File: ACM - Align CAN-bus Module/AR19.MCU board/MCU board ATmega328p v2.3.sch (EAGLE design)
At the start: 39 parts, among them IC1 ATMEGA328P-MMH, IC2 MIC5239-5.0YS_TR, IC3 MCP25625-E_ML, J1 AVR_SPI_PROG_3X2NS

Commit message: Ryddet og la til den nye krystallen
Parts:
- removed QF1, QF2: 16M20AUM1, crystal:16M20AUM1
- added U$1, U$2: FA-20H, FA-20H 16.0000MF20X-B:FA-20H
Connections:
- net CAN_OSC1: now also U$1.1; no longer QF2.1
- net CAN_OSC2: now also U$1.3; no longer QF2.3
- net GND: no longer QF1.2, QF2.2
- net MCU_OSC1: now also U$2.1; no longer QF1.1
- net MCU_OSC2: now also U$2.3; no longer QF1.3
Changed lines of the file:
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@@
 <part name="C2" library="12066D106KAT2A" deviceset="12066D106KAT2A" device="" value="22pF"/>
 <part name="C3" library="12066D106KAT2A" deviceset="12066D106KAT2A" device="" value="22pF"/>
-<part name="GND1" library="supply1" library_urn="urn:adsk.eagle:library:371" deviceset="GND" device=""/>
 <part name="GND2" library="supply1" library_urn="urn:adsk.eagle:library:371" deviceset="GND" device=""/>
 <part name="P_I/O6" library="wirepad" library_urn="urn:adsk.eagle:library:412" deviceset="2,15/1,0" device="" package3d_urn="urn:adsk.eagle:package:30831/1"/>
@@
 <part name="GND5" library="supply1" library_urn="urn:adsk.eagle:library:371" deviceset="GND" device=""/>
 <part name="GND6" library="supply1" library_urn="urn:adsk.eagle:library:371" deviceset="GND" device=""/>
-<part name="QF1" library="crystal" library_urn="urn:adsk.eagle:library:204" deviceset="16M20AUM1" device="" package3d_urn="urn:adsk.eagle:package:12117/1"/>
 <part name="CAN_H" library="wirepad" library_urn="urn:adsk.eagle:library:412" deviceset="2,15/1,0" device="" package3d_urn="urn:adsk.eagle:package:30831/1"/>
 <part name="CAN_L" library="wirepad" library_urn="urn:adsk.eagle:library:412" deviceset="2,15/1,0" device="" package3d_urn="urn:adsk.eagle:package:30831/1"/>
@@
 <part name="C9" library="12066D106KAT2A" deviceset="12066D106KAT2A" device="" value="22pF"/>
 <part name="C10" library="12066D106KAT2A" deviceset="12066D106KAT2A" device="" value="22pF"/>
-<part name="GND19" library="supply1" library_urn="urn:adsk.eagle:library:371" deviceset="GND" device=""/>
-<part name="QF2" library="crystal" library_urn="urn:adsk.eagle:library:204" deviceset="16M20AUM1" device="" package3d_urn="urn:adsk.eagle:package:12117/1"/>
 <part name="GND20" library="supply1" library_urn="urn:adsk.eagle:library:371" deviceset="GND" device=""/>
 <part name="GND21" library="supply1" library_urn="urn:adsk.eagle:library:371" deviceset="GND" device=""/>
+<part name="U$1" library="FA-20H 16.0000MF20X-B" deviceset="FA-20H" device=""/>
+<part name="U$2" library="FA-20H 16.0000MF20X-B" deviceset="FA-20H" device=""/>
 </parts>
 <sheets>
@@
 <attribute name="VALUE" x="354.33" y="95.25" size="1.778" layer="96" rot="R180" align="center-left"/>
 </instance>
-<instance part="GND1" gate="1" x="332.74" y="81.28" smashed="yes">
-<attribute name="VALUE" x="330.2" y="78.74" size="1.778" layer="96"/>
-</instance>
 <instance part="GND2" gate="1" x="-22.86" y="142.24" smashed="yes">
 <attribute name="VALUE" x="-25.4" y="139.7" size="1.778" layer="96"/>
@@
 <attribute name="VALUE" x="-27.94" y="139.7" size="1.778" layer="96" rot="MR0"/>
 </instance>
-<instance part="QF1" gate="G$1" x="332.74" y="101.6" smashed="yes">
-<attribute name="NAME" x="332.74" y="110.236" size="1.778" layer="95"/>
-<attribute name="VALUE" x="332.74" y="106.68" size="1.778" layer="96"/>
-</instance>
 <instance part="CAN_H" gate="1" x="238.76" y="5.08" smashed="yes" rot="R180">
 <attribute name="NAME" x="239.903" y="8.3058" size="1.778" layer="95" rot="R180"/>
@@
 <attribute name="VALUE" x="349.25" y="57.15" size="1.778" layer="96" align="center-left"/>
 </instance>
-<instance part="GND19" gate="1" x="332.74" y="48.26" smashed="yes">
-<attribute name="VALUE" x="330.2" y="45.72" size="1.778" layer="96"/>
-</instance>
-<instance part="QF2" gate="G$1" x="332.74" y="68.58" smashed="yes">
-<attribute name="NAME" x="335.28" y="69.596" size="1.778" layer="95"/>
-<attribute name="VALUE" x="335.28" y="66.04" size="1.778" layer="96"/>
-</instance>
 <instance part="GND20" gate="1" x="320.04" y="48.26" smashed="yes">
 <attribute name="VALUE" x="317.5" y="45.72" size="1.778" layer="96"/>
@@
 <attribute name="VALUE" x="342.9" y="45.72" size="1.778" layer="96"/>
 </instance>
+<instance part="U$1" gate="G$1" x="363.22" y="55.88" smashed="yes"/>
+<instance part="U$2" gate="G$1" x="363.22" y="88.9" smashed="yes"/>
 </instances>
 <busses>
@@
 </segment>
 <segment>
-<pinref part="GND1" gate="1" pin="GND"/>
-<pinref part="QF1" gate="G$1" pin="2"/>
-<wire x1="332.74" y1="83.82" x2="332.74" y2="96.52" width="0.1524" layer="91"/>
-</segment>
-<segment>
 <pinref part="C2" gate="G$1" pin="1"/>
 <pinref part="GND17" gate="1" pin="GND"/>
@@
 <pinref part="GND18" gate="1" pin="GND"/>
 <wire x1="345.44" y1="86.36" x2="345.44" y2="83.82" width="0.1524" layer="91"/>
-</segment>
-<segment>
-<pinref part="GND19" gate="1" pin="GND"/>
-<pinref part="QF2" gate="G$1" pin="2"/>
-<wire x1="332.74" y1="50.8" x2="332.74" y2="63.5" width="0.1524" layer="91"/>
 </segment>
 <segment>
@@
 <pinref part="C2" gate="G$1" pin="2"/>
 <label x="314.96" y="101.6" size="1.778" layer="95" rot="R180"/>
-<pinref part="QF1" gate="G$1" pin="1"/>
 <wire x1="320.04" y1="99.06" x2="320.04" y2="101.6" width="0.1524" layer="91"/>
-<wire x1="320.04" y1="101.6" x2="330.2" y2="101.6" width="0.1524" layer="91"/>
 <wire x1="320.04" y1="101.6" x2="314.96" y2="101.6" width="0.1524" layer="91"/>
+<pinref part="U$2" gate="G$1" pin="1"/>
+<wire x1="320.04" y1="101.6" x2="322.58" y2="101.6" width="0.1524" layer="91"/>
 <junction x="320.04" y="101.6"/>
 </segment>
@@
 <pinref part="C3" gate="G$1" pin="2"/>
 <label x="350.52" y="101.6" size="1.778" layer="95" rot="MR180"/>
-<pinref part="QF1" gate="G$1" pin="3"/>
 <wire x1="345.44" y1="99.06" x2="345.44" y2="101.6" width="0.1524" layer="91"/>
-<wire x1="345.44" y1="101.6" x2="335.28" y2="101.6" width="0.1524" layer="91"/>
 <wire x1="345.44" y1="101.6" x2="350.52" y2="101.6" width="0.1524" layer="91"/>
+<pinref part="U$2" gate="G$1" pin="3"/>
+<wire x1="339.09" y1="101.6" x2="345.44" y2="101.6" width="0.1524" layer="91"/>
 <junction x="345.44" y="101.6"/>
 </segment>
@@
 <pinref part="C9" gate="G$1" pin="2"/>
 <label x="314.96" y="68.58" size="1.778" layer="95" rot="R180"/>
-<pinref part="QF2" gate="G$1" pin="1"/>
 <wire x1="320.04" y1="66.04" x2="320.04" y2="68.58" width="0.1524" layer="91"/>
-<wire x1="320.04" y1="68.58" x2="330.2" y2="68.58" width="0.1524" layer="91"/>
 <wire x1="320.04" y1="68.58" x2="314.96" y2="68.58" width="0.1524" layer="91"/>
+<pinref part="U$1" gate="G$1" pin="1"/>
+<wire x1="322.58" y1="68.58" x2="320.04" y2="68.58" width="0.1524" layer="91"/>
 <junction x="320.04" y="68.58"/>
 </segment>
@@
 <pinref part="C10" gate="G$1" pin="2"/>
 <label x="350.52" y="68.58" size="1.778" layer="95" rot="MR180"/>
-<pinref part="QF2" gate="G$1" pin="3"/>
 <wire x1="345.44" y1="66.04" x2="345.44" y2="68.58" width="0.1524" layer="91"/>
-<wire x1="345.44" y1="68.58" x2="335.28" y2="68.58" width="0.1524" layer="91"/>
 <wire x1="345.44" y1="68.58" x2="350.52" y2="68.58" width="0.1524" layer="91"/>
+<pinref part="U$1" gate="G$1" pin="3"/>
+<wire x1="339.09" y1="68.58" x2="345.44" y2="68.58" width="0.1524" layer="91"/>
 <junction x="345.44" y="68.58"/>
 </segment>

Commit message: Pakket og klart
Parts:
- removed U$1, U$2: FA-20H, FA-20H 16.0000MF20X-B:FA-20H
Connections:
- net CAN_OSC1: no longer U$1.1
- net CAN_OSC2: no longer U$1.3
- net MCU_OSC1: no longer U$2.1
- net MCU_OSC2: no longer U$2.3
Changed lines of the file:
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@@
 <part name="GND20" library="supply1" library_urn="urn:adsk.eagle:library:371" deviceset="GND" device=""/>
 <part name="GND21" library="supply1" library_urn="urn:adsk.eagle:library:371" deviceset="GND" device=""/>
-<part name="U$1" library="FA-20H 16.0000MF20X-B" deviceset="FA-20H" device=""/>
-<part name="U$2" library="FA-20H 16.0000MF20X-B" deviceset="FA-20H" device=""/>
 </parts>
 <sheets>
@@
 <attribute name="VALUE" x="342.9" y="45.72" size="1.778" layer="96"/>
 </instance>
-<instance part="U$1" gate="G$1" x="363.22" y="55.88" smashed="yes"/>
-<instance part="U$2" gate="G$1" x="363.22" y="88.9" smashed="yes"/>
 </instances>
 <busses>
@@
 <label x="314.96" y="101.6" size="1.778" layer="95" rot="R180"/>
 <wire x1="320.04" y1="99.06" x2="320.04" y2="101.6" width="0.1524" layer="91"/>
+<wire x1="320.04" y1="101.6" x2="330.2" y2="101.6" width="0.1524" layer="91"/>
 <wire x1="320.04" y1="101.6" x2="314.96" y2="101.6" width="0.1524" layer="91"/>
-<pinref part="U$2" gate="G$1" pin="1"/>
-<wire x1="320.04" y1="101.6" x2="322.58" y2="101.6" width="0.1524" layer="91"/>
 <junction x="320.04" y="101.6"/>
 </segment>
@@
 <label x="350.52" y="101.6" size="1.778" layer="95" rot="MR180"/>
 <wire x1="345.44" y1="99.06" x2="345.44" y2="101.6" width="0.1524" layer="91"/>
+<wire x1="345.44" y1="101.6" x2="335.28" y2="101.6" width="0.1524" layer="91"/>
 <wire x1="345.44" y1="101.6" x2="350.52" y2="101.6" width="0.1524" layer="91"/>
-<pinref part="U$2" gate="G$1" pin="3"/>
-<wire x1="339.09" y1="101.6" x2="345.44" y2="101.6" width="0.1524" layer="91"/>
 <junction x="345.44" y="101.6"/>
 </segment>
@@
 <label x="314.96" y="68.58" size="1.778" layer="95" rot="R180"/>
 <wire x1="320.04" y1="66.04" x2="320.04" y2="68.58" width="0.1524" layer="91"/>
+<wire x1="320.04" y1="68.58" x2="330.2" y2="68.58" width="0.1524" layer="91"/>
 <wire x1="320.04" y1="68.58" x2="314.96" y2="68.58" width="0.1524" layer="91"/>
-<pinref part="U$1" gate="G$1" pin="1"/>
-<wire x1="322.58" y1="68.58" x2="320.04" y2="68.58" width="0.1524" layer="91"/>
 <junction x="320.04" y="68.58"/>
 </segment>
@@
 <label x="350.52" y="68.58" size="1.778" layer="95" rot="MR180"/>
 <wire x1="345.44" y1="66.04" x2="345.44" y2="68.58" width="0.1524" layer="91"/>
+<wire x1="345.44" y1="68.58" x2="335.28" y2="68.58" width="0.1524" layer="91"/>
 <wire x1="345.44" y1="68.58" x2="350.52" y2="68.58" width="0.1524" layer="91"/>
-<pinref part="U$1" gate="G$1" pin="3"/>
-<wire x1="339.09" y1="68.58" x2="345.44" y2="68.58" width="0.1524" layer="91"/>
 <junction x="345.44" y="68.58"/>
 </segment>

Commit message: Created BOM 031018
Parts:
- added U$1, U$2: FA-20H, FA-20H 16.0000MF20X-B:FA-20H
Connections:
- net CAN_OSC1: now also U$1.1
- net CAN_OSC2: now also U$1.3
- net MCU_OSC1: now also U$2.1
- net MCU_OSC2: now also U$2.3
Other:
- moved on the sheet: C10, C2, C3, C9
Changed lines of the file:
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@@
 <part name="GND20" library="supply1" library_urn="urn:adsk.eagle:library:371" deviceset="GND" device=""/>
 <part name="GND21" library="supply1" library_urn="urn:adsk.eagle:library:371" deviceset="GND" device=""/>
+<part name="U$1" library="FA-20H 16.0000MF20X-B" deviceset="FA-20H" device=""/>
+<part name="U$2" library="FA-20H 16.0000MF20X-B" deviceset="FA-20H" device=""/>
 </parts>
 <sheets>
@@
 <attribute name="VALUE" x="85.217" y="146.558" size="1.778" layer="96"/>
 </instance>
-<instance part="C2" gate="G$1" x="320.04" y="86.36" smashed="yes" rot="R90">
-<attribute name="NAME" x="316.23" y="92.71" size="1.778" layer="95" rot="R180" align="center-left"/>
-<attribute name="VALUE" x="316.23" y="95.25" size="1.778" layer="96" rot="R180" align="center-left"/>
-</instance>
-<instance part="C3" gate="G$1" x="345.44" y="86.36" smashed="yes" rot="R90">
-<attribute name="NAME" x="351.79" y="92.71" size="1.778" layer="95" rot="R180" align="center-left"/>
-<attribute name="VALUE" x="354.33" y="95.25" size="1.778" layer="96" rot="R180" align="center-left"/>
+<instance part="C2" gate="G$1" x="322.58" y="86.36" smashed="yes" rot="R90">
+<attribute name="NAME" x="318.77" y="92.71" size="1.778" layer="95" rot="R180" align="center-left"/>
+<attribute name="VALUE" x="318.77" y="95.25" size="1.778" layer="96" rot="R180" align="center-left"/>
+</instance>
+<instance part="C3" gate="G$1" x="350.52" y="86.36" smashed="yes" rot="R90">
+<attribute name="NAME" x="356.87" y="92.71" size="1.778" layer="95" rot="R180" align="center-left"/>
+<attribute name="VALUE" x="359.41" y="95.25" size="1.778" layer="96" rot="R180" align="center-left"/>
 </instance>
 <instance part="GND2" gate="1" x="-22.86" y="142.24" smashed="yes">
@@
 <attribute name="VALUE" x="226.06" y="27.94" size="1.778" layer="96"/>
 </instance>
-<instance part="GND17" gate="1" x="320.04" y="81.28" smashed="yes">
-<attribute name="VALUE" x="317.5" y="78.74" size="1.778" layer="96"/>
-</instance>
-<instance part="GND18" gate="1" x="345.44" y="81.28" smashed="yes">
-<attribute name="VALUE" x="342.9" y="78.74" size="1.778" layer="96"/>
-</instance>
-<instance part="C9" gate="G$1" x="320.04" y="53.34" smashed="yes" rot="R90">
-<attribute name="NAME" x="316.23" y="59.69" size="1.778" layer="95" rot="R180" align="center-left"/>
-<attribute name="VALUE" x="316.23" y="57.15" size="1.778" layer="96" rot="R180" align="center-left"/>
-</instance>
-<instance part="C10" gate="G$1" x="345.44" y="53.34" smashed="yes" rot="R90">
-<attribute name="NAME" x="349.25" y="59.69" size="1.778" layer="95" align="center-left"/>
-<attribute name="VALUE" x="349.25" y="57.15" size="1.778" layer="96" align="center-left"/>
-</instance>
-<instance part="GND20" gate="1" x="320.04" y="48.26" smashed="yes">
-<attribute name="VALUE" x="317.5" y="45.72" size="1.778" layer="96"/>
-</instance>
-<instance part="GND21" gate="1" x="345.44" y="48.26" smashed="yes">
-<attribute name="VALUE" x="342.9" y="45.72" size="1.778" layer="96"/>
-</instance>
+<instance part="GND17" gate="1" x="322.58" y="81.28" smashed="yes">
+<attribute name="VALUE" x="320.04" y="78.74" size="1.778" layer="96"/>
+</instance>
+<instance part="GND18" gate="1" x="350.52" y="81.28" smashed="yes">
+<attribute name="VALUE" x="347.98" y="78.74" size="1.778" layer="96"/>
+</instance>
+<instance part="C9" gate="G$1" x="322.58" y="45.72" smashed="yes" rot="R90">
+<attribute name="NAME" x="318.77" y="52.07" size="1.778" layer="95" rot="R180" align="center-left"/>
+<attribute name="VALUE" x="318.77" y="49.53" size="1.778" layer="96" rot="R180" align="center-left"/>
+</instance>
+<instance part="C10" gate="G$1" x="350.52" y="45.72" smashed="yes" rot="R90">
+<attribute name="NAME" x="354.33" y="52.07" size="1.778" layer="95" align="center-left"/>
+<attribute name="VALUE" x="354.33" y="49.53" size="1.778" layer="96" align="center-left"/>
+</instance>
+<instance part="GND20" gate="1" x="322.58" y="40.64" smashed="yes">
+<attribute name="VALUE" x="320.04" y="38.1" size="1.778" layer="96"/>
+</instance>
+<instance part="GND21" gate="1" x="350.52" y="40.64" smashed="yes">
+<attribute name="VALUE" x="347.98" y="38.1" size="1.778" layer="96"/>
+</instance>
+<instance part="U$1" gate="G$1" x="337.82" y="58.42" smashed="yes"/>
+<instance part="U$2" gate="G$1" x="335.28" y="99.06" smashed="yes"/>
 </instances>
 <busses>
@@
 <pinref part="C2" gate="G$1" pin="1"/>
 <pinref part="GND17" gate="1" pin="GND"/>
-<wire x1="320.04" y1="86.36" x2="320.04" y2="83.82" width="0.1524" layer="91"/>
+<wire x1="322.58" y1="86.36" x2="322.58" y2="83.82" width="0.1524" layer="91"/>
 </segment>
 <segment>
 <pinref part="C3" gate="G$1" pin="1"/>
 <pinref part="GND18" gate="1" pin="GND"/>
-<wire x1="345.44" y1="86.36" x2="345.44" y2="83.82" width="0.1524" layer="91"/>
+<wire x1="350.52" y1="86.36" x2="350.52" y2="83.82" width="0.1524" layer="91"/>
 </segment>
 <segment>
 <pinref part="C9" gate="G$1" pin="1"/>
 <pinref part="GND20" gate="1" pin="GND"/>
-<wire x1="320.04" y1="53.34" x2="320.04" y2="50.8" width="0.1524" layer="91"/>
+<wire x1="322.58" y1="45.72" x2="322.58" y2="43.18" width="0.1524" layer="91"/>
 </segment>
 <segment>
 <pinref part="C10" gate="G$1" pin="1"/>
 <pinref part="GND21" gate="1" pin="GND"/>
-<wire x1="345.44" y1="53.34" x2="345.44" y2="50.8" width="0.1524" layer="91"/>
+<wire x1="350.52" y1="45.72" x2="350.52" y2="43.18" width="0.1524" layer="91"/>
 </segment>
 </net>
@@
 <segment>
 <pinref part="C2" gate="G$1" pin="2"/>
-<label x="314.96" y="101.6" size="1.778" layer="95" rot="R180"/>
-<wire x1="320.04" y1="99.06" x2="320.04" y2="101.6" width="0.1524" layer="91"/>
-<wire x1="320.04" y1="101.6" x2="330.2" y2="101.6" width="0.1524" layer="91"/>
-<wire x1="320.04" y1="101.6" x2="314.96" y2="101.6" width="0.1524" layer="91"/>
-<junction x="320.04" y="101.6"/>
+<label x="317.5" y="101.6" size="1.778" layer="95" rot="R180"/>
+<wire x1="322.58" y1="99.06" x2="322.58" y2="101.6" width="0.1524" layer="91"/>
+<wire x1="322.58" y1="101.6" x2="317.5" y2="101.6" width="0.1524" layer="91"/>
+<pinref part="U$2" gate="G$1" pin="1"/>
+<wire x1="327.04" y1="101.06" x2="327.04" y2="101.6" width="0.1524" layer="91"/>
+<wire x1="327.04" y1="101.6" x2="322.58" y2="101.6" width="0.1524" layer="91"/>
+<junction x="322.58" y="101.6"/>
 </segment>
 </net>
@@
 <segment>
 <pinref part="C3" gate="G$1" pin="2"/>
-<label x="350.52" y="101.6" size="1.778" layer="95" rot="MR180"/>
-<wire x1="345.44" y1="99.06" x2="345.44" y2="101.6" width="0.1524" layer="91"/>
-<wire x1="345.44" y1="101.6" x2="335.28" y2="101.6" width="0.1524" layer="91"/>
-<wire x1="345.44" y1="101.6" x2="350.52" y2="101.6" width="0.1524" layer="91"/>
-<junction x="345.44" y="101.6"/>
+<label x="355.6" y="101.6" size="1.778" layer="95" rot="MR180"/>
+<wire x1="350.52" y1="99.06" x2="350.52" y2="101.6" width="0.1524" layer="91"/>
+<wire x1="350.52" y1="101.6" x2="355.6" y2="101.6" width="0.1524" layer="91"/>
+<pinref part="U$2" gate="G$1" pin="3"/>
+<wire x1="343.55" y1="101.06" x2="343.55" y2="101.6" width="0.1524" layer="91"/>
+<wire x1="343.55" y1="101.6" x2="350.52" y2="101.6" width="0.1524" layer="91"/>
+<junction x="350.52" y="101.6"/>
 </segment>
 </net>
@@
 <segment>
 <pinref part="C9" gate="G$1" pin="2"/>
-<label x="314.96" y="68.58" size="1.778" layer="95" rot="R180"/>
-<wire x1="320.04" y1="66.04" x2="320.04" y2="68.58" width="0.1524" layer="91"/>
-<wire x1="320.04" y1="68.58" x2="330.2" y2="68.58" width="0.1524" layer="91"/>
-<wire x1="320.04" y1="68.58" x2="314.96" y2="68.58" width="0.1524" layer="91"/>
-<junction x="320.04" y="68.58"/>
+<label x="317.5" y="60.96" size="1.778" layer="95" rot="R180"/>
+<wire x1="322.58" y1="58.42" x2="322.58" y2="60.96" width="0.1524" layer="91"/>
+<wire x1="322.58" y1="60.96" x2="317.5" y2="60.96" width="0.1524" layer="91"/>
+<pinref part="U$1" gate="G$1" pin="1"/>
+<wire x1="329.58" y1="60.42" x2="329.58" y2="60.96" width="0.1524" layer="91"/>
+<wire x1="329.58" y1="60.96" x2="322.58" y2="60.96" width="0.1524" layer="91"/>
+<junction x="322.58" y="60.96"/>
 </segment>
 </net>
@@
 <segment>
 <pinref part="C10" gate="G$1" pin="2"/>
-<label x="350.52" y="68.58" size="1.778" layer="95" rot="MR180"/>
-<wire x1="345.44" y1="66.04" x2="345.44" y2="68.58" width="0.1524" layer="91"/>
-<wire x1="345.44" y1="68.58" x2="335.28" y2="68.58" width="0.1524" layer="91"/>
-<wire x1="345.44" y1="68.58" x2="350.52" y2="68.58" width="0.1524" layer="91"/>
-<junction x="345.44" y="68.58"/>
-</segment>
-</net>
+<label x="355.6" y="60.96" size="1.778" layer="95" rot="MR180"/>
+<wire x1="350.52" y1="58.42" x2="350.52" y2="60.96" width="0.1524" layer="91"/>
+<wire x1="350.52" y1="60.96" x2="355.6" y2="60.96" width="0.1524" layer="91"/>
+<pinref part="U$1" gate="G$1" pin="3"/>
+<wire x1="346.09" y1="60.42" x2="346.09" y2="60.96" width="0.1524" layer="91"/>
+<wire x1="346.09" y1="60.96" x2="350.52" y2="60.96" width="0.1524" layer="91"/>
+<junction x="350.52" y="60.96"/>
+</segment>
+</net>

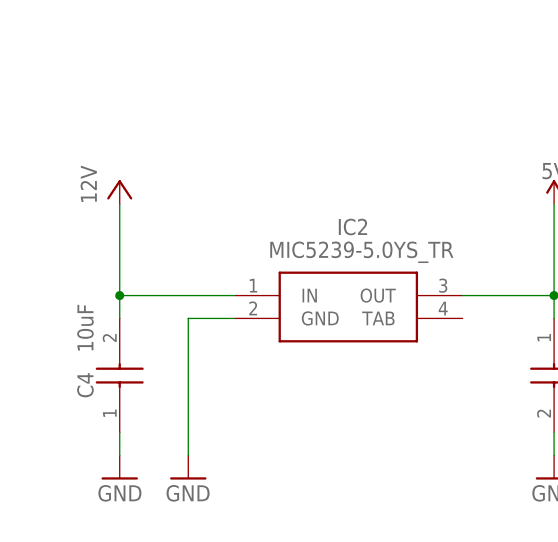
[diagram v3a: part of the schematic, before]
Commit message: Added: Fuse Block (Littelfuse SMD fuse block)
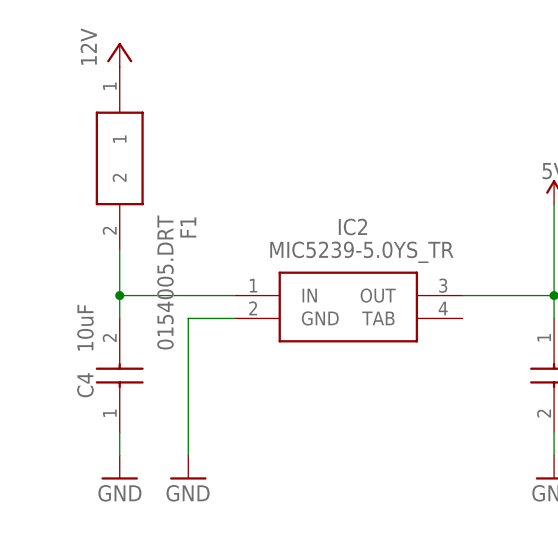
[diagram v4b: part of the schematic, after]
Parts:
- added F1: 0154005.DRT, 0154005(Fuseholder)DRT:0154005.DRT
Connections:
- new net N$2: C4.A, F1.2, IC2.IN
- net VCC: now also F1.1; no longer C4.A, IC2.IN
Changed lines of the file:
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@@
 <part name="U$1" library="FA-20H 16.0000MF20X-B" deviceset="FA-20H" device=""/>
 <part name="U$2" library="FA-20H 16.0000MF20X-B" deviceset="FA-20H" device=""/>
+<part name="F1" library="0154005(Fuseholder)DRT" deviceset="0154005.DRT" device=""/>
 </parts>
 <sheets>
@@
 <attribute name="VALUE" x="220.98" y="66.04" size="1.778" layer="96"/>
 </instance>
-<instance part="P+2" gate="VCC" x="-30.48" y="175.26" smashed="yes">
-<attribute name="VALUE" x="-33.02" y="172.72" size="1.778" layer="96" rot="R90"/>
+<instance part="P+2" gate="VCC" x="-30.48" y="190.5" smashed="yes">
+<attribute name="VALUE" x="-33.02" y="187.96" size="1.778" layer="96" rot="R90"/>
 </instance>
 <instance part="SUPPLY1" gate="G$1" x="2.54" y="53.34" smashed="yes" rot="R90">
@@
 <instance part="U$1" gate="G$1" x="337.82" y="58.42" smashed="yes"/>
 <instance part="U$2" gate="G$1" x="335.28" y="99.06" smashed="yes"/>
+<instance part="F1" gate="G$1" x="-30.48" y="187.96" smashed="yes" rot="R270">
+<attribute name="NAME" x="-22.86" y="171.45" size="1.778" layer="95" rot="R270" align="center-left"/>
+<attribute name="VALUE" x="-25.4" y="171.45" size="1.778" layer="96" rot="R270" align="center-left"/>
+</instance>
 </instances>
 <busses>
@@
 </segment>
 <segment>
-<pinref part="C4" gate="G$1" pin="A"/>
-<pinref part="IC2" gate="G$1" pin="IN"/>
-<wire x1="-30.48" y1="160.02" x2="-30.48" y2="162.56" width="0.1524" layer="91"/>
 <pinref part="P+2" gate="VCC" pin="VCC"/>
-<wire x1="-30.48" y1="162.56" x2="-17.78" y2="162.56" width="0.1524" layer="91"/>
-<wire x1="-30.48" y1="172.72" x2="-30.48" y2="162.56" width="0.1524" layer="91"/>
-<junction x="-30.48" y="162.56"/>
+<pinref part="F1" gate="G$1" pin="1"/>
 </segment>
 </net>
@@
 </segment>
 </net>
+<net name="N$2" class="0">
+<segment>
+<pinref part="F1" gate="G$1" pin="2"/>
+<pinref part="C4" gate="G$1" pin="A"/>
+<wire x1="-30.48" y1="167.64" x2="-30.48" y2="162.56" width="0.1524" layer="91"/>
+<pinref part="IC2" gate="G$1" pin="IN"/>
+<wire x1="-30.48" y1="162.56" x2="-30.48" y2="160.02" width="0.1524" layer="91"/>
+<wire x1="-17.78" y1="162.56" x2="-30.48" y2="162.56" width="0.1524" layer="91"/>
+<junction x="-30.48" y="162.56"/>
+</segment>
+</net>
